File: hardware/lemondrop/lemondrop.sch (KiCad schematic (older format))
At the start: 109 parts, among them P1 RX_SMA, P2 TX_SMA, P3 SPI, P4 POWER, P5 ADC/DAC, P6 XCVR_CTL, P7 CLOCK_CTL, P8 GSG-SMA-CONN, P9 CONN_2, T1 RX_BALUN, T2 TX_BALUN, U1 MAX5864, U2 MAX2837, U3 SI5351C, X1 GSG-XTAL4PIN

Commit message: 1V8 option in schematic
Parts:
- added K? (x5): CONN_3, symbol CONN_3
- added P11: 1V8, symbol CONN_3X2
- added R37, R40, R41: 120, symbol R
- added R38, R39: 100, symbol R
- P4: value POWER -> VCC
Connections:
- net CLK: now also P5.39 (P39), R37.2; no longer C44.2, C45.1
- net GND: now also P11.1, P11.3, P11.5, R37.1, R40.2, R41.2
- net VCC: now also K?.1 (P1), K?.1 (P1), K?.1 (P1), K?.1 (P1), K?.1 (P1); no longer C31.1, C32.1, C46.1, C47.1, C49.1, C50.1, U1.18 (OVDD)
- net at R20.2: now also C44.2, C45.1; no longer P5.39 (P39)
- net DIN renamed DIN_XCVR
- net DIN_XCVR: now also R38.1; no longer U1.34 (DIN)
- net DOUT renamed DOUT_XCVR
- net SCLK renamed SCLK_XCVR
- net SCLK_XCVR: now also R39.1; no longer U1.35 (SCLK)
- new net +1.8V: K?.3 (P3), K?.3 (P3), K?.3 (P3), K?.3 (P3), K?.3 (P3), P11.2, P11.4, P11.6
- new net DIN_AD: R38.2, R40.1, U1.34 (DIN)
- new net OVDD: C31.1, C32.1, K?.2 (PM), U1.18 (OVDD)
- new net SCLK_AD: R39.2, R41.1, U1.35 (SCLK)
- new net VDDOA: C50.1, K?.2 (PM)
- new net VDDOB: C49.1, K?.2 (PM)
- new net VDDOC: C47.1, K?.2 (PM)
- new net VDDOD: C46.1, K?.2 (PM)
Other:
- note added: "Install R37 only if 1.8 V\noutput is desired and VDDOA\nis set to VCC."
- note added: "Install R40 and R41 only\nif 1V8 is used for U1."
- note added: "Use jumper to select U1 I/O voltage."
- note added: "Use jumpers to select clock output voltage."
- note added: "optional 1V8 input"
- moved on the sheet: C25, C26, C27, C28, C29, C30, C31, C32, C46, C47, C48, C49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

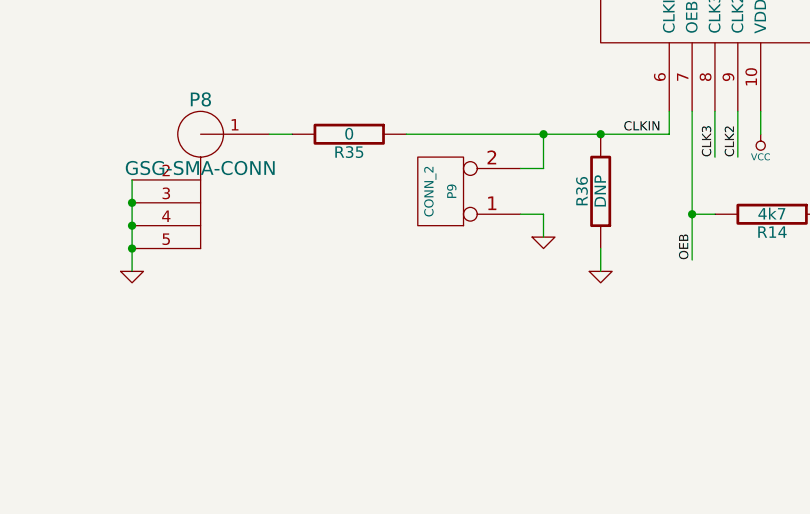
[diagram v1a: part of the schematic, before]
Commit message: clock input ground note
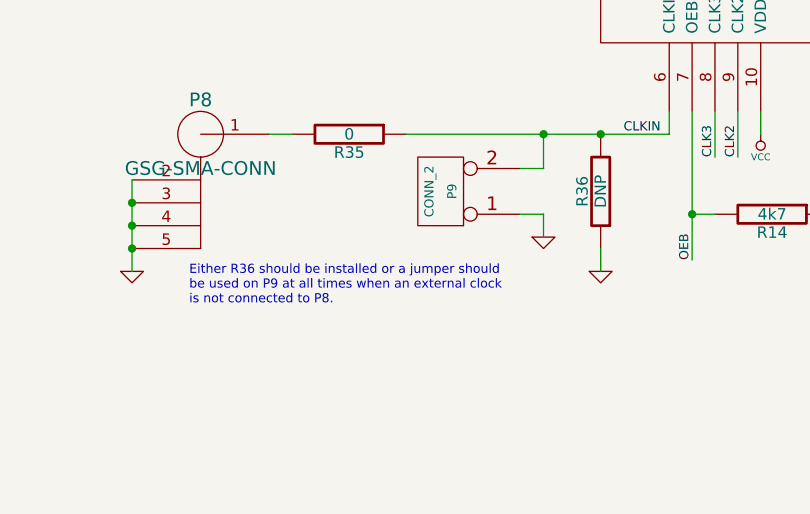
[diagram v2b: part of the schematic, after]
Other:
- note added: "Either R36 should be installed or a jumper should\nbe used on P9 at all times when an external clock\nis not connected to P8."
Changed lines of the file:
@@
-EESchema Schematic File Version 2  date Sat May  5 10:58:55 2012
+EESchema Schematic File Version 2  date Sat May  5 11:07:56 2012
 LIBS:power
 LIBS:device
@@
 Comment4 ""
 $EndDescr
+Text Notes 2200 9600 0    40   ~ 0
+Either R36 should be installed or a jumper should\nbe used on P9 at all times when an external clock\nis not connected to P8.
 Wire Notes Line
 	11000 8600 11000 7400

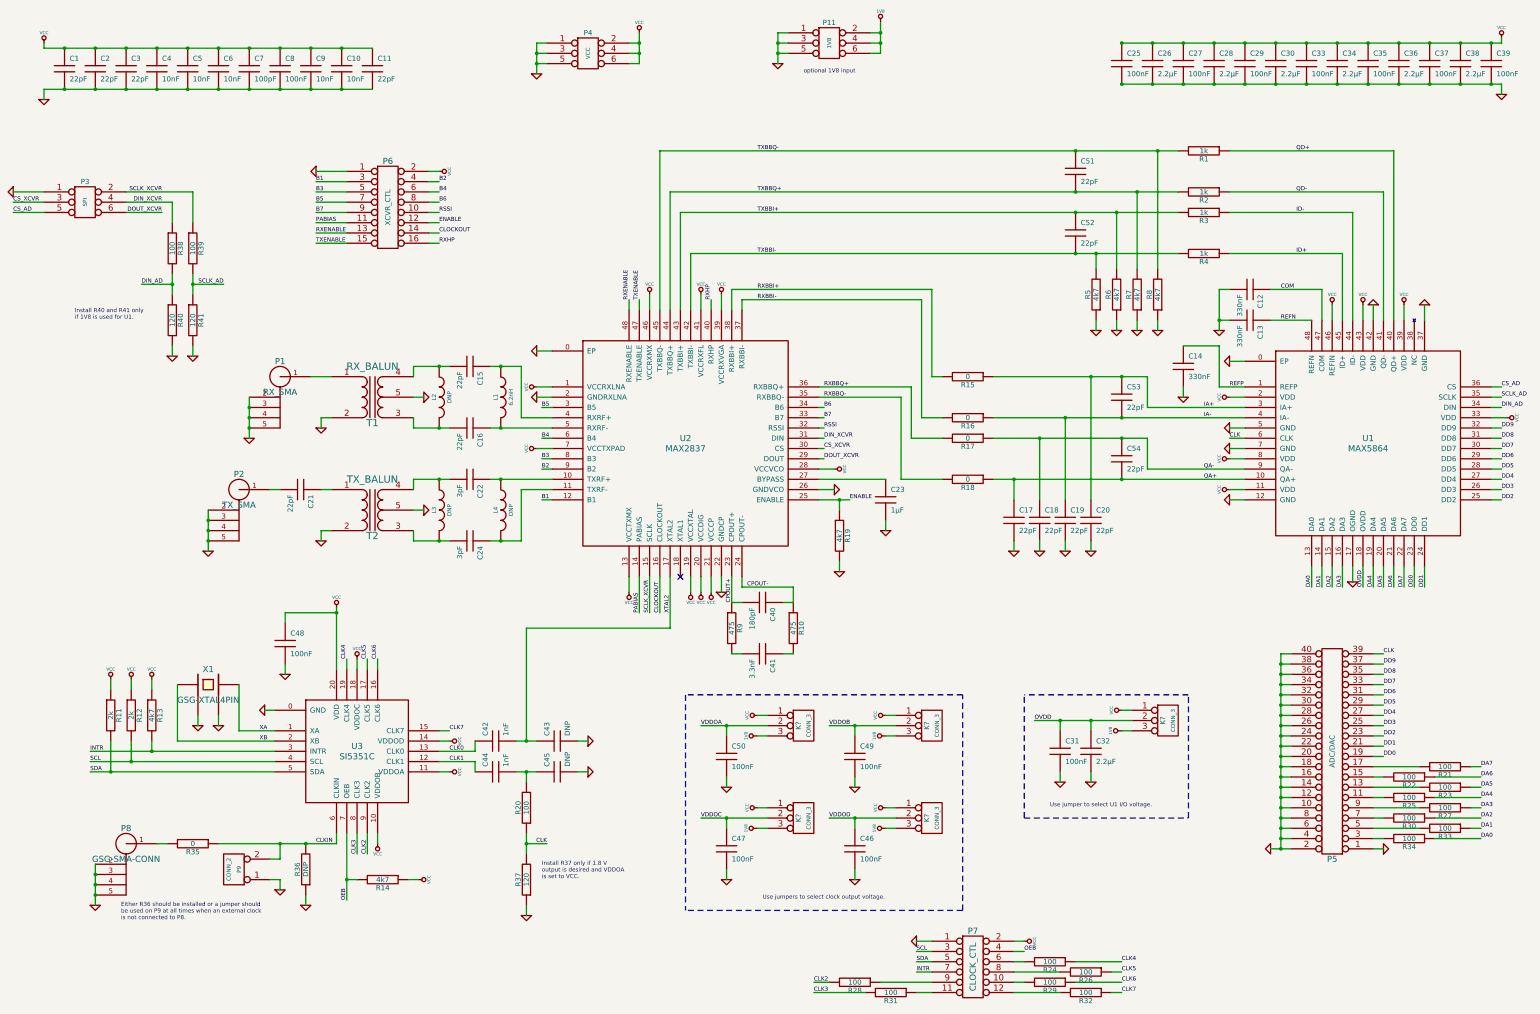
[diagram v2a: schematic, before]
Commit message: fixed VDDOx
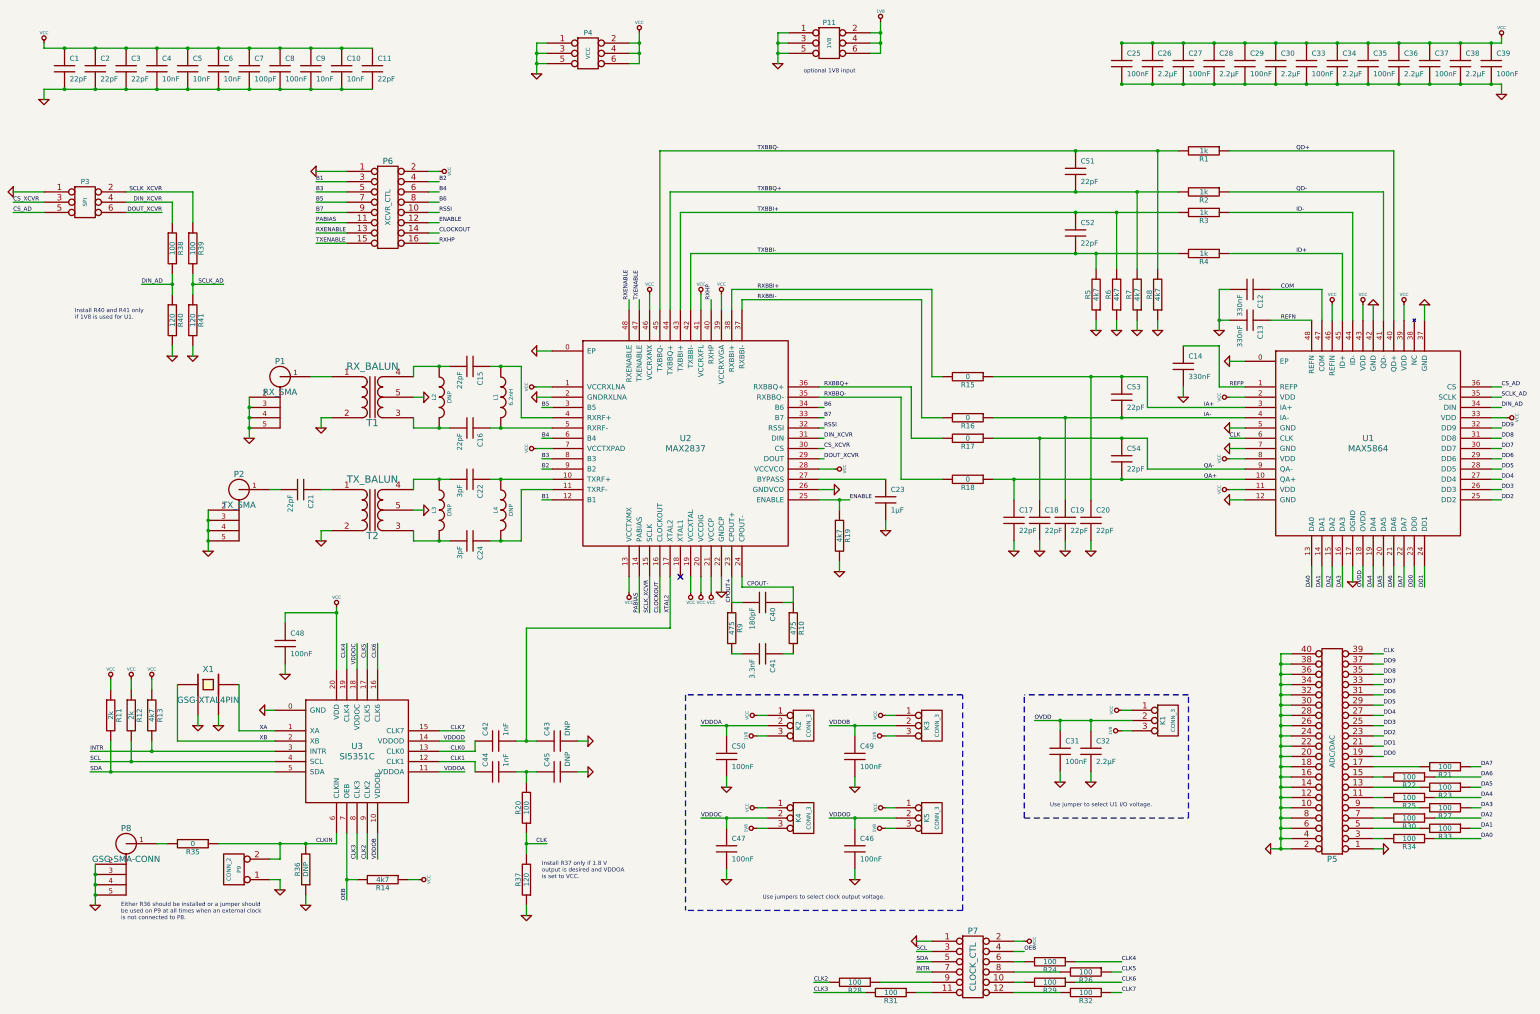
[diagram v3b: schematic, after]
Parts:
- gave numbers to parts that had none: 5
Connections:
- net VCC: no longer U3.10 (VDDOB), U3.11 (VDDOA), U3.14 (VDDOD), U3.18 (VDDOC)
- net VDDOA: now also U3.11 (VDDOA)
- net VDDOB: now also U3.10 (VDDOB)
- net VDDOC: now also U3.18 (VDDOC)
- net VDDOD: now also U3.14 (VDDOD)

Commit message: started layout updates
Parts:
- renumbered K2 to P?, K3 to P?, K5 to P?, K4 to P?, K1 to P?

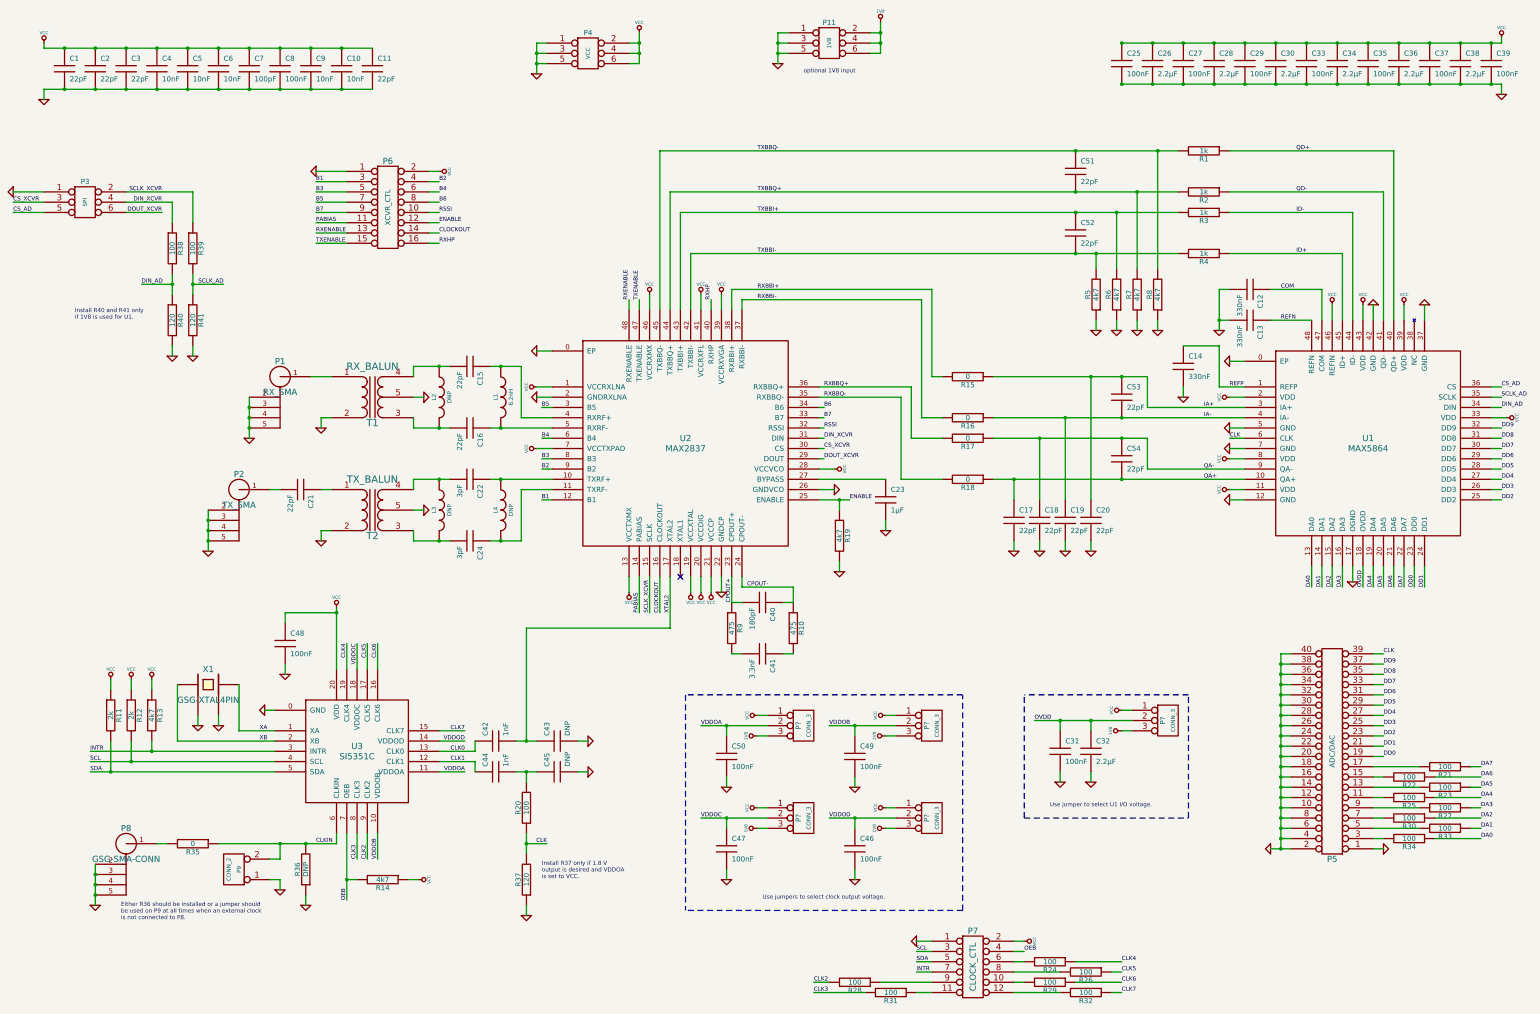
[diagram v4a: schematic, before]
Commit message: fixed balun pin order
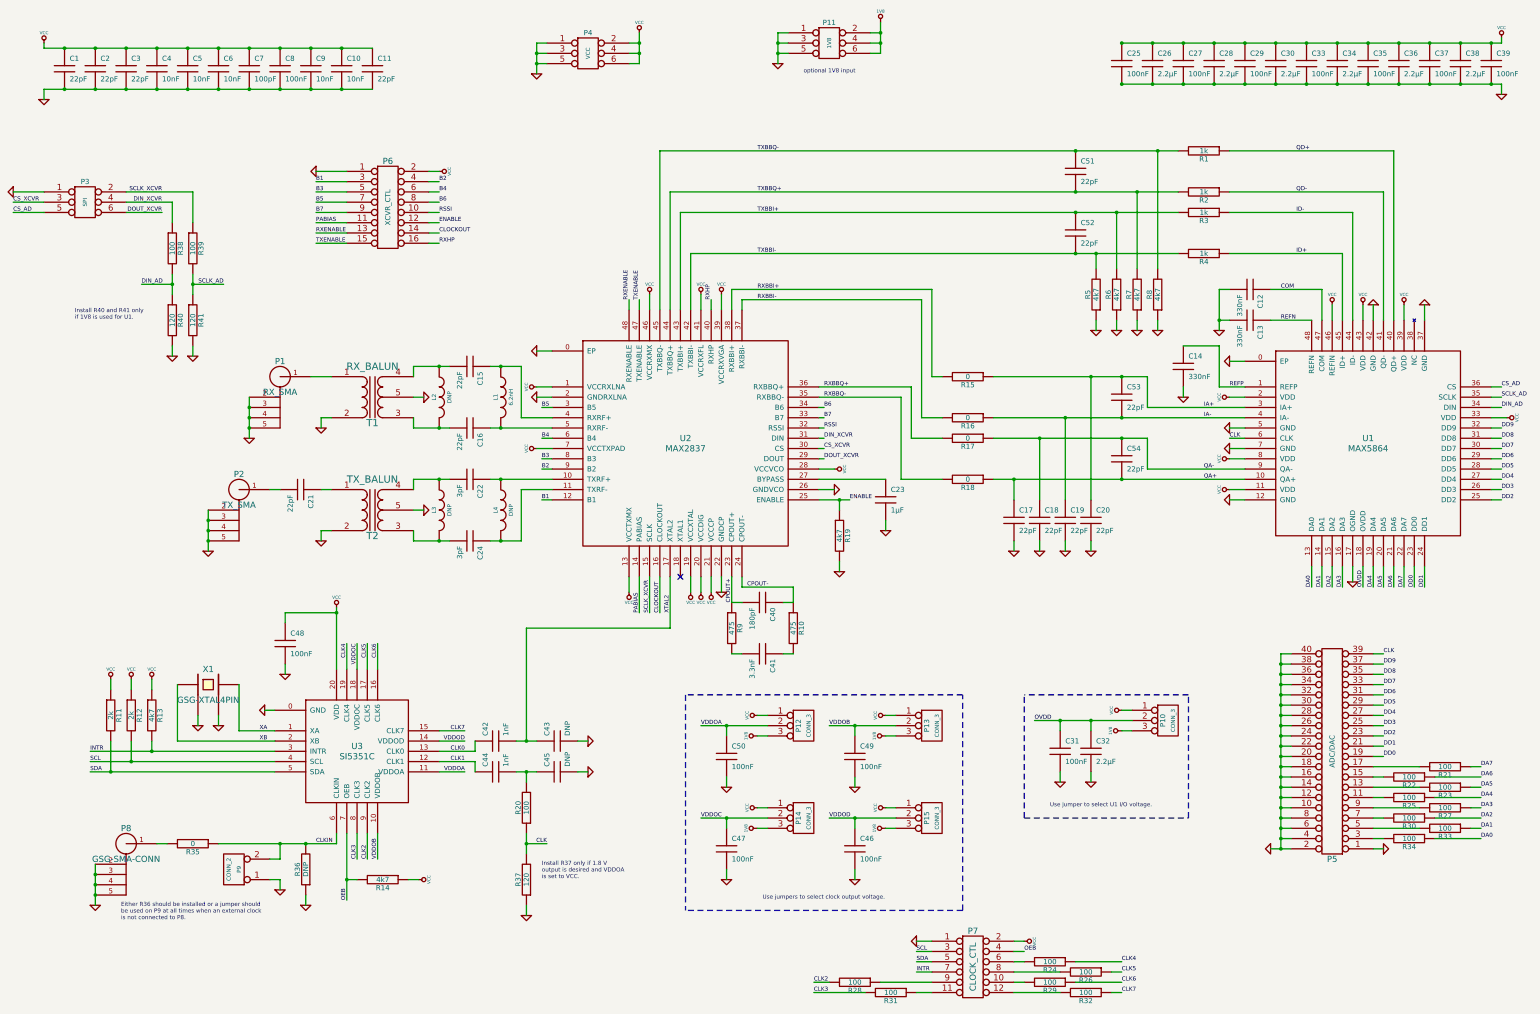
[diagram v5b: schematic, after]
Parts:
- gave numbers to parts that had none: 5

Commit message: corrected crystal selection
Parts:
- X1: Description CRYSTAL 27.000000 MHZ 8PF SMD -> CRYSTAL 25 MHZ 10.00PF SMD; Part Number NX3225SA-27.000000MHZ -> NX3225SA-25.000000MHZ
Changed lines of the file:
@@
-EESchema Schematic File Version 2  date Sun May  6 16:07:31 2012
+EESchema Schematic File Version 2  date Fri Jul 13 13:08:49 2012
 LIBS:power
 LIBS:device
@@
 Sheet 1 1
 Title "lemondrop"
-Date "6 may 2012"
+Date "13 jul 2012"
 Rev ""
 Comp "Copyright 2012 Michael Ossmann"
@@
 F 1 "GSG-XTAL4PIN" H 3050 7150 60  0000 C CNN
 F 4 "NDK" H 3050 7300 60  0001 C CNN "Manufacturer"
-F 5 "NX3225SA-27.000000MHZ" H 3050 7300 60  0001 C CNN "Part Number"
-F 6 "CRYSTAL 27.000000 MHZ 8PF SMD" H 3050 7300 60  0001 C CNN "Description"
+F 5 "NX3225SA-25.000000MHZ" H 3050 7300 60  0001 C CNN "Part Number"
+F 6 "CRYSTAL 25 MHZ 10.00PF SMD" H 3050 7300 60  0001 C CNN "Description"
 	1    3050 7300
 	1    0    0    -1
